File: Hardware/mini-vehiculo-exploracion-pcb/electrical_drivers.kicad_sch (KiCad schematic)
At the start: 0 parts

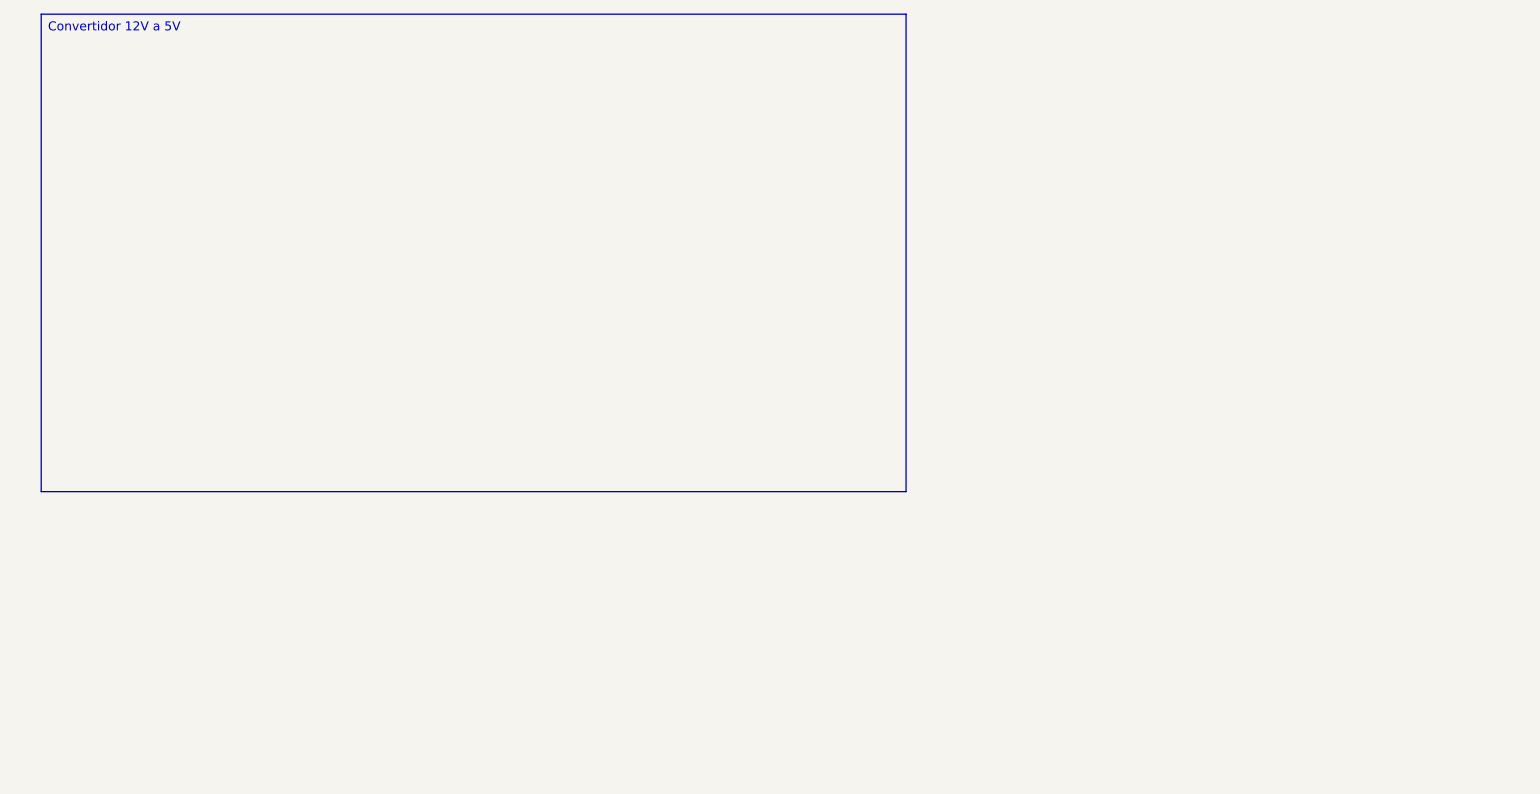
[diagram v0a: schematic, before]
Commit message: reductores de voltaje drivers
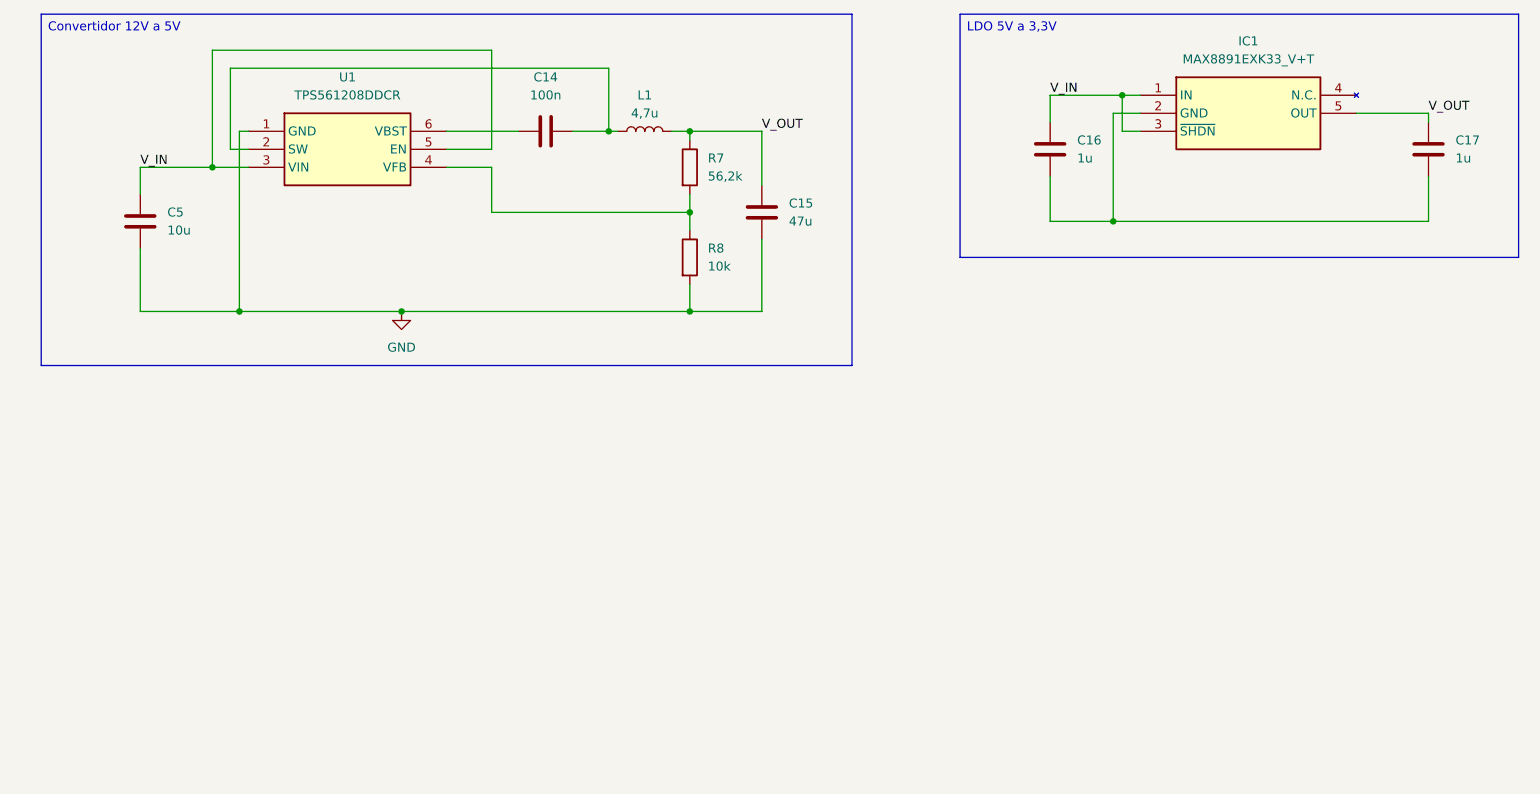
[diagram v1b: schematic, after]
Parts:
- added C14: 100n, symbol Device:C
- added C15: 47u, symbol Device:C
- added C16, C17: 1u, symbol Device:C
- added C5: 10u, symbol Device:C
- added IC1: MAX8891EXK33_V+T, SOT65P210X110-5N, symbol MAX8891EXK33_V+T:MAX8891EXK33_V+T
- added L1: 4,7u, symbol Device:L
- added R7: 56,2k, symbol Device:R
- added R8: 10k, symbol Device:R
- added U1: TPS561208DDCR, SOT95P280X110-6N, symbol TPS561208DDCR:TPS561208DDCR
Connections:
- new net: R7.2, R8.1, U1.4 (VFB)
- new net: C16.2, C17.2, IC1.2 (GND)
- new net: C14.2, L1.1, U1.2 (SW)
- new net: C14.1, U1.6 (VBST)
- new net GND: C15.2, C5.2, R8.2, U1.1 (GND)
- new net V_IN: C16.1, C5.1, IC1.1 (IN), IC1.3 (~{SHDN}), U1.3 (VIN), U1.5 (EN)
- new net V_OUT: C15.1, C17.1, IC1.5 (OUT), L1.2, R7.1

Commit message: conclusion electrical drivers
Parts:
- added D1: PTVS13VP1UTP-QX, SODFL4725X110N, symbol PTVS13VP1UTP-QX:PTVS13VP1UTP-QX
- added D2: D_Schottky, symbol Device:D_Schottky
- added F1: SMD200F_24-2920-2, SMD200F2429202, symbol SMD200F_24-2920-2:SMD200F_24-2920-2
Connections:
- net GND: now also D1.2 (A)
- net V_IN: now also D1.1 (K), F1.1
- net V_OUT: now also D2.1 (K)
- new net: D2.2 (A), F1.2

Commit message: actualizacion labels pcb drivers
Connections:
- removed net V_IN: C16.1, C5.1, D1.1 (K), F1.1, IC1.1 (IN), IC1.3 (~{SHDN}), U1.3 (VIN), U1.5 (EN)
- net V_OUT renamed +5V
- net +5V: now also C16.1, IC1.1 (IN), IC1.3 (~{SHDN}); no longer C17.1, D2.1 (K), IC1.5 (OUT)
- new net +12V: C5.1, D2.1 (K), U1.3 (VIN), U1.5 (EN)
- new net +3.3V: C17.1, IC1.5 (OUT)
- new net V_BAT: D1.1 (K), F1.1
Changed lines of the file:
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@@
 	(text_box "proteccion entrada bateria"
 		(exclude_from_sim no)
-		(at 22.86 85.09 0)
-		(size 68.58 45.72)
+		(at 17.78 85.09 0)
+		(size 73.66 45.72)
 		(margins 0.9525 0.9525 0.9525 0.9525)
 		(stroke
@@
 	)
 	(junction
+		(at 163.83 34.29)
+		(diameter 0)
+		(color 0 0 0 0)
+	)
+	(junction
 		(at 49.53 64.77)
 		(diameter 0)
@@
 	)
 	(junction
+		(at 123.19 39.37)
+		(diameter 0)
+		(color 0 0 0 0)
+	)
+	(junction
 		(at 113.03 64.77)
 		(diameter 0)
@@
 	)
 	(junction
+		(at 101.6 39.37)
+		(diameter 0)
+		(color 0 0 0 0)
+	)
+	(junction
+		(at 35.56 44.45)
+		(diameter 0)
+		(color 0 0 0 0)
+	)
+	(junction
+		(at 217.17 36.83)
+		(diameter 0)
+		(color 0 0 0 0)
+	)
+	(junction
+		(at 45.72 44.45)
+		(diameter 0)
+		(color 0 0 0 0)
+	)
+	(junction
+		(at 172.72 52.07)
+		(diameter 0)
+		(color 0 0 0 0)
+	)
+	(junction
+		(at 113.03 39.37)
+		(diameter 0)
+		(color 0 0 0 0)
+	)
+	(junction
 		(at 31.75 96.52)
 		(diameter 0)
@@
 	)
 	(junction
-		(at 101.6 39.37)
-		(diameter 0)
-		(color 0 0 0 0)
-	)
-	(junction
-		(at 45.72 44.45)
-		(diameter 0)
-		(color 0 0 0 0)
-	)
-	(junction
-		(at 172.72 52.07)
-		(diameter 0)
-		(color 0 0 0 0)
-	)
-	(junction
-		(at 113.03 39.37)
-		(diameter 0)
-		(color 0 0 0 0)
-	)
-	(junction
 		(at 113.03 50.8)
 		(diameter 0)
@@
 	(wire
 		(pts
+			(xy 31.75 44.45) (xy 35.56 44.45)
+		)
+		(stroke
+			(width 0)
+			(type default)
+		)
+	)
+	(wire
+		(pts
 			(xy 45.72 27.94) (xy 45.72 44.45)
 		)
@@
 	(wire
 		(pts
+			(xy 123.19 39.37) (xy 127 39.37)
+		)
+		(stroke
+			(width 0)
+			(type default)
+		)
+	)
+	(wire
+		(pts
+			(xy 27.94 96.52) (xy 31.75 96.52)
+		)
+		(stroke
+			(width 0)
+			(type default)
+		)
+	)
+	(wire
+		(pts
 			(xy 72.39 64.77) (xy 113.03 64.77)
 		)
@@
 	(wire
 		(pts
+			(xy 160.02 34.29) (xy 163.83 34.29)
+		)
+		(stroke
+			(width 0)
+			(type default)
+		)
+	)
+	(wire
+		(pts
 			(xy 172.72 36.83) (xy 172.72 52.07)
 		)
@@
 	(wire
 		(pts
-			(xy 74.93 96.52) (xy 85.09 96.52)
+			(xy 74.93 96.52) (xy 82.55 96.52)
 		)
 		(stroke
@@
 	(wire
 		(pts
-			(xy 26.67 96.52) (xy 31.75 96.52)
-		)
-		(stroke
-			(width 0)
-			(type default)
-		)
-	)
-	(wire
-		(pts
 			(xy 31.75 115.57) (xy 31.75 119.38)
 		)
@@
 	(wire
 		(pts
+			(xy 217.17 36.83) (xy 220.98 36.83)
+		)
+		(stroke
+			(width 0)
+			(type default)
+		)
+	)
+	(wire
+		(pts
 			(xy 85.09 41.91) (xy 85.09 27.94)
 		)
@@
 		)
 	)
-	(label "V_IN"
-		(at 35.56 44.45 0)
+	(global_label "+5V"
+		(shape input)
+		(at 127 39.37 0)
+		(fields_autoplaced yes)
 		(effects
 			(font
 				(size 1.27 1.27)
 			)
-			(justify left bottom)
-		)
-	)
-	(label "V_OUT"
-		(at 85.09 96.52 0)
+			(justify left)
+		)
+		(property "Intersheetrefs" "${INTERSHEET_REFS}"
+			(at 133.8557 39.37 0)
+			(effects
+				(font
+					(size 1.27 1.27)
+				)
+				(justify left)
+				(hide yes)
+			)
+		)
+	)
+	(global_label "+12V"
+		(shape input)
+		(at 82.55 96.52 0)
+		(fields_autoplaced yes)
 		(effects
 			(font
 				(size 1.27 1.27)
 			)
-			(justify left bottom)
-		)
-	)
-	(label "V_IN"
-		(at 163.83 34.29 0)
+			(justify left)
+		)
+		(property "Intersheetrefs" "${INTERSHEET_REFS}"
+			(at 90.6152 96.52 0)
+			(effects
+				(font
+					(size 1.27 1.27)
+				)
+				(justify left)
+				(hide yes)
+			)
+		)
+	)
+	(global_label "+3.3V"
+		(shape input)
+		(at 220.98 36.83 0)
+		(fields_autoplaced yes)
 		(effects
 			(font
 				(size 1.27 1.27)
 			)
-			(justify left bottom)
-		)
-	)
-	(label "V_OUT"
-		(at 217.17 36.83 0)
+			(justify left)
+		)
+		(property "Intersheetrefs" "${INTERSHEET_REFS}"
+			(at 229.65 36.83 0)
+			(effects
+				(font
+					(size 1.27 1.27)
+				)
+				(justify left)
+				(hide yes)
+			)
+		)
+	)
+	(global_label "+5V"
+		(shape input)
+		(at 160.02 34.29 180)
+		(fields_autoplaced yes)
 		(effects
 			(font
 				(size 1.27 1.27)
 			)
-			(justify left bottom)
-		)
-	)
-	(label "V_IN"
-		(at 26.67 96.52 0)
+			(justify right)
+		)
+		(property "Intersheetrefs" "${INTERSHEET_REFS}"
+			(at 153.1643 34.29 0)
+			(effects
+				(font
+					(size 1.27 1.27)
+				)
+				(justify right)
+				(hide yes)
+			)
+		)
+	)
+	(global_label "V_BAT"
+		(shape input)
+		(at 27.94 96.52 180)
+		(fields_autoplaced yes)
 		(effects
 			(font
 				(size 1.27 1.27)
 			)
-			(justify left bottom)
-		)
-	)
-	(label "V_OUT"
-		(at 123.19 39.37 0)
+			(justify right)
+		)
+		(property "Intersheetrefs" "${INTERSHEET_REFS}"
+			(at 19.5724 96.52 0)
+			(effects
+				(font
+					(size 1.27 1.27)
+				)
+				(justify right)
+				(hide yes)
+			)
+		)
+	)
+	(global_label "+12V"
+		(shape input)
+		(at 31.75 44.45 180)
+		(fields_autoplaced yes)
 		(effects
 			(font
 				(size 1.27 1.27)
 			)
-			(justify left bottom)
-		)
-	)
+			(justify right)
+		)
+		(property "Intersheetrefs" "${INTERSHEET_REFS}"
+			(at 23.6848 44.45 0)
+			(effects
+				(font
+					(size 1.27 1.27)
+				)
+				(justify right)
+				(hide yes)
+			)
+		)
+	)

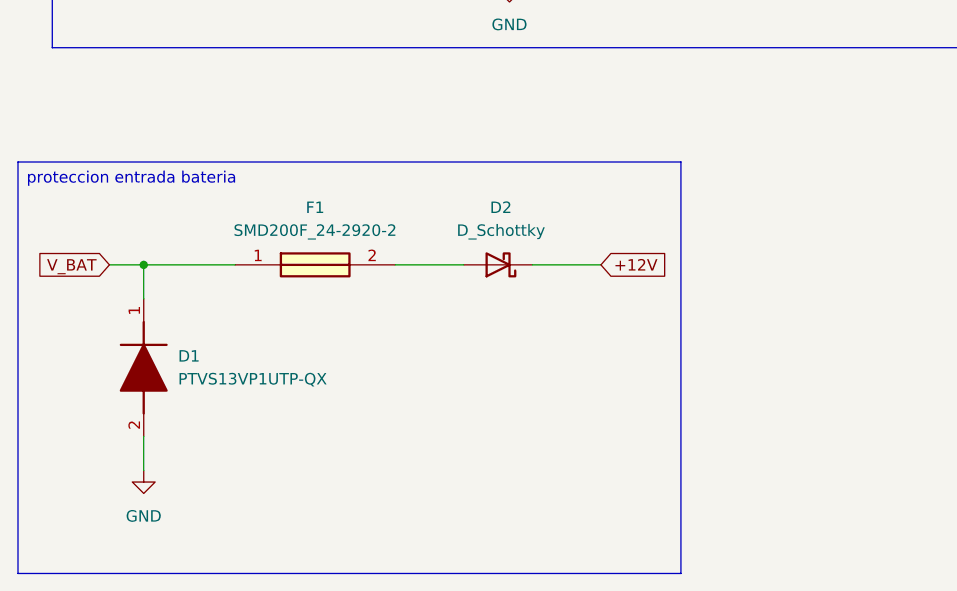
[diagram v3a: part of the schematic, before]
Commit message: reemplazo diodo schottky drivers
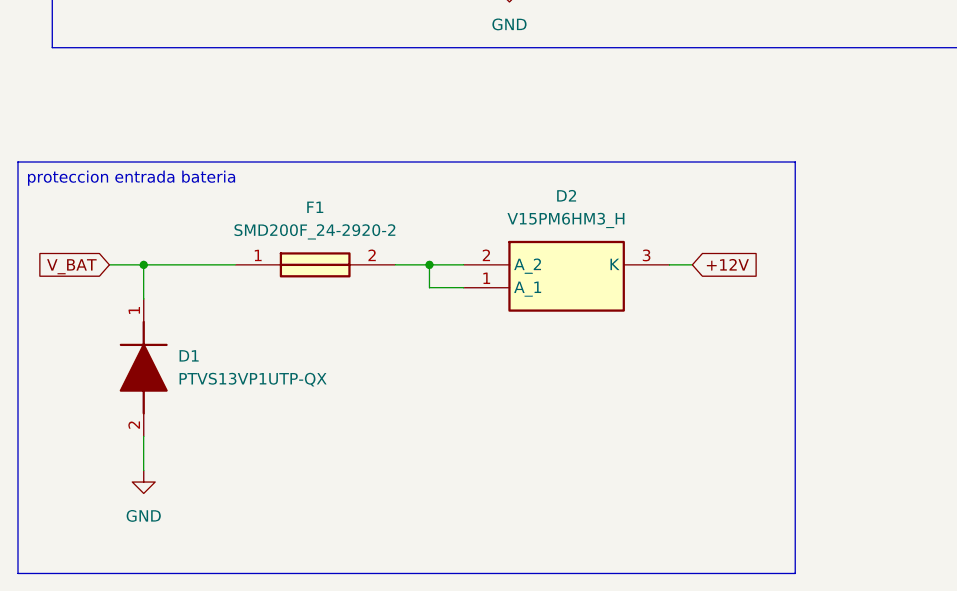
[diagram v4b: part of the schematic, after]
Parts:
- removed D2: D_Schottky, symbol Device:D_Schottky
- added D2: V15PM6HM3_H, V15PM6HM3H, symbol V15PM6HM3_H:V15PM6HM3_H
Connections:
- net +12V: now also D2.3 (K)
- net at F1.2: now also D2.1 (A_1), D2.2 (A_2)
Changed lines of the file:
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@@
 		(exclude_from_sim no)
 		(at 17.78 85.09 0)
-		(size 73.66 45.72)
+		(size 86.36 45.72)
 		(margins 0.9525 0.9525 0.9525 0.9525)
 		(stroke
@@
 	)
 	(junction
+		(at 63.5 96.52)
+		(diameter 0)
+		(color 0 0 0 0)
+	)
+	(junction
 		(at 72.39 64.77)
 		(diameter 0)
@@
 	(wire
 		(pts
+			(xy 67.31 99.06) (xy 63.5 99.06)
+		)
+		(stroke
+			(width 0)
+			(type default)
+		)
+	)
+	(wire
+		(pts
 			(xy 173.99 34.29) (xy 173.99 39.37)
 		)
@@
 	(wire
 		(pts
-			(xy 74.93 96.52) (xy 82.55 96.52)
-		)
-		(stroke
-			(width 0)
-			(type default)
-		)
-	)
-	(wire
-		(pts
-			(xy 59.69 96.52) (xy 67.31 96.52)
+			(xy 59.69 96.52) (xy 63.5 96.52)
 		)
 		(stroke
@@
 	(wire
 		(pts
+			(xy 90.17 96.52) (xy 92.71 96.52)
+		)
+		(stroke
+			(width 0)
+			(type default)
+		)
+	)
+	(wire
+		(pts
 			(xy 172.72 52.07) (xy 217.17 52.07)
 		)
@@
 	(wire
 		(pts
+			(xy 63.5 96.52) (xy 67.31 96.52)
+		)
+		(stroke
+			(width 0)
+			(type default)
+		)
+	)
+	(wire
+		(pts
 			(xy 31.75 96.52) (xy 41.91 96.52)
 		)
@@
 		(pts
 			(xy 85.09 50.8) (xy 113.03 50.8)
+		)
+		(stroke
+			(width 0)
+			(type default)
+		)
+	)
+	(wire
+		(pts
+			(xy 63.5 96.52) (xy 63.5 99.06)
 		)
 		(stroke
@@
 	(global_label "+12V"
 		(shape input)
-		(at 82.55 96.52 0)
+		(at 92.71 96.52 0)
 		(fields_autoplaced yes)
 		(effects
@@
 		)
 		(property "Intersheetrefs" "${INTERSHEET_REFS}"
-			(at 90.6152 96.52 0)
+			(at 100.7752 96.52 0)
 			(effects
 				(font
@@
 	)
 	(symbol
-		(lib_id "Device:D_Schottky")
-		(at 71.12 96.52 180)
-		(unit 1)
-		(exclude_from_sim no)
-		(in_bom yes)
-		(on_board yes)
-		(dnp no)
-		(fields_autoplaced yes)
-		(property "Reference" "D2"
-			(at 71.4375 90.17 0)
-			(effects
-				(font
-					(size 1.27 1.27)
-				)
-			)
-		)
-		(property "Value" "D_Schottky"
-			(at 71.4375 92.71 0)
-			(effects
-				(font
-					(size 1.27 1.27)
-				)
-			)
-		)
-		(property "Footprint" ""
-			(at 71.12 96.52 0)
-			(effects
-				(font
-					(size 1.27 1.27)
-				)
-				(hide yes)
-			)
-		)
-		(property "Datasheet" "~"
-			(at 71.12 96.52 0)
-			(effects
-				(font
-					(size 1.27 1.27)
-				)
-				(hide yes)
-			)
-		)
-		(property "Description" "Schottky diode"
-			(at 71.12 96.52 0)
-			(effects
-				(font
-					(size 1.27 1.27)
-				)
-				(hide yes)
-			)
-		)
-		(pin "1"
-		)
-		(pin "2"
-		)
-		(instances
-			(project ""
-				(path "/7776e3ee-622a-4a3e-a213-279f6f5df2cb/a0a3a615-a0eb-4e9b-a594-71f734cb4e88"
-					(reference "D2")
-					(unit 1)
-				)
-			)
-		)
-	)
-	(symbol
 		(lib_id "Device:C")
 		(at 217.17 41.91 0)
@@
 					(unit 1)
 				)
+			)
+		)
+	)
+	(symbol
+		(lib_id "V15PM6HM3_H:V15PM6HM3_H")
+		(at 67.31 96.52 0)
+		(unit 1)
+		(exclude_from_sim no)
+		(in_bom yes)
+		(on_board yes)
+		(dnp no)
+		(fields_autoplaced yes)
+		(property "Reference" "D2"
+			(at 78.74 88.9 0)
+			(effects
+				(font
+					(size 1.27 1.27)
+				)
+			)
+		)
+		(property "Value" "V15PM6HM3_H"
+			(at 78.74 91.44 0)
+			(effects
+				(font
+					(size 1.27 1.27)
+				)
+			)
+		)
+		(property "Footprint" "V15PM6HM3H"
+			(at 86.36 191.44 0)
+			(effects
+				(font
+					(size 1.27 1.27)
+				)
+				(justify left top)
+				(hide yes)
+			)
+		)
+		(property "Datasheet" "https://www.vishay.com/docs/87434/v15pm6.pdf"
+			(at 86.36 291.44 0)
+			(effects
+				(font
+					(size 1.27 1.27)
+				)
+				(justify left top)
+				(hide yes)
+			)
+		)
+		(property "Description" "Schottky Diodes & Rectifiers 60V 15A TMBS TO-277A (SMPC)"
+			(at 67.31 96.52 0)
+			(effects
+				(font
+					(size 1.27 1.27)
+				)
+				(hide yes)
+			)
+		)
+		(property "Height" "1.2"
+			(at 86.36 491.44 0)
+			(effects
+				(font
+					(size 1.27 1.27)
+				)
+				(justify left top)
+				(hide yes)
+			)
+		)
+		(property "Mouser Part Number" "78-V15PM6HM3/H"
+			(at 86.36 591.44 0)
+			(effects
+				(font
+					(size 1.27 1.27)
+				)
+				(justify left top)
+				(hide yes)
+			)
+		)
+		(property "Mouser Price/Stock" "https://www.mouser.co.uk/ProductDetail/Vishay-General-Semiconductor/V15PM6HM3-H?qs=gZXFycFWdANWPtpgGjtwuA%3D%3D"
+			(at 86.36 691.44 0)
+			(effects
+				(font
+					(size 1.27 1.27)
+				)
+				(justify left top)
+				(hide yes)
+			)
+		)
+		(property "Manufacturer_Name" "Vishay"
+			(at 86.36 791.44 0)
+			(effects
+				(font
+					(size 1.27 1.27)
+				)
+				(justify left top)
+				(hide yes)
+			)
+		)
+		(property "Manufacturer_Part_Number" "V15PM6HM3/H"
+			(at 86.36 891.44 0)
+			(effects
+				(font
+					(size 1.27 1.27)
+				)
+				(justify left top)
+				(hide yes)
+			)
+		)
+		(pin "1"
+		)
+		(pin "3"
+		)
+		(pin "2"
+		)
+		(instances
+			(project ""
+				(path "/7776e3ee-622a-4a3e-a213-279f6f5df2cb/a0a3a615-a0eb-4e9b-a594-71f734cb4e88"
+					(reference "D2")
+					(unit 1)
+				)
